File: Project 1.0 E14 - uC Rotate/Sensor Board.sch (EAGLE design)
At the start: 106 parts, among them IC1 LT1963EST-1.5, IC2 LT1963EST-1.5, IC4 LT1963EST-1.5, J1 501568-0207, J2 501568-0207, J3 SD-105027-101, J4 501568-0407, U1 MAG3110, U10 ADXL362, U11 TM4C1233H6PM, U14 TXB0108, U15 ADT7301, U17 LSM9DS0, U19 MAX21000, U2 H3LIS331DLTR, U21 SN74HC42, U22 SI7013, U3 L3GD20H, U4 LPS331AP, U5 MPL3115A2, U6 LSM303D, U8 STLM20, U9 LIS3DH, X1 32.768 kHz, X2 16.000 MHz

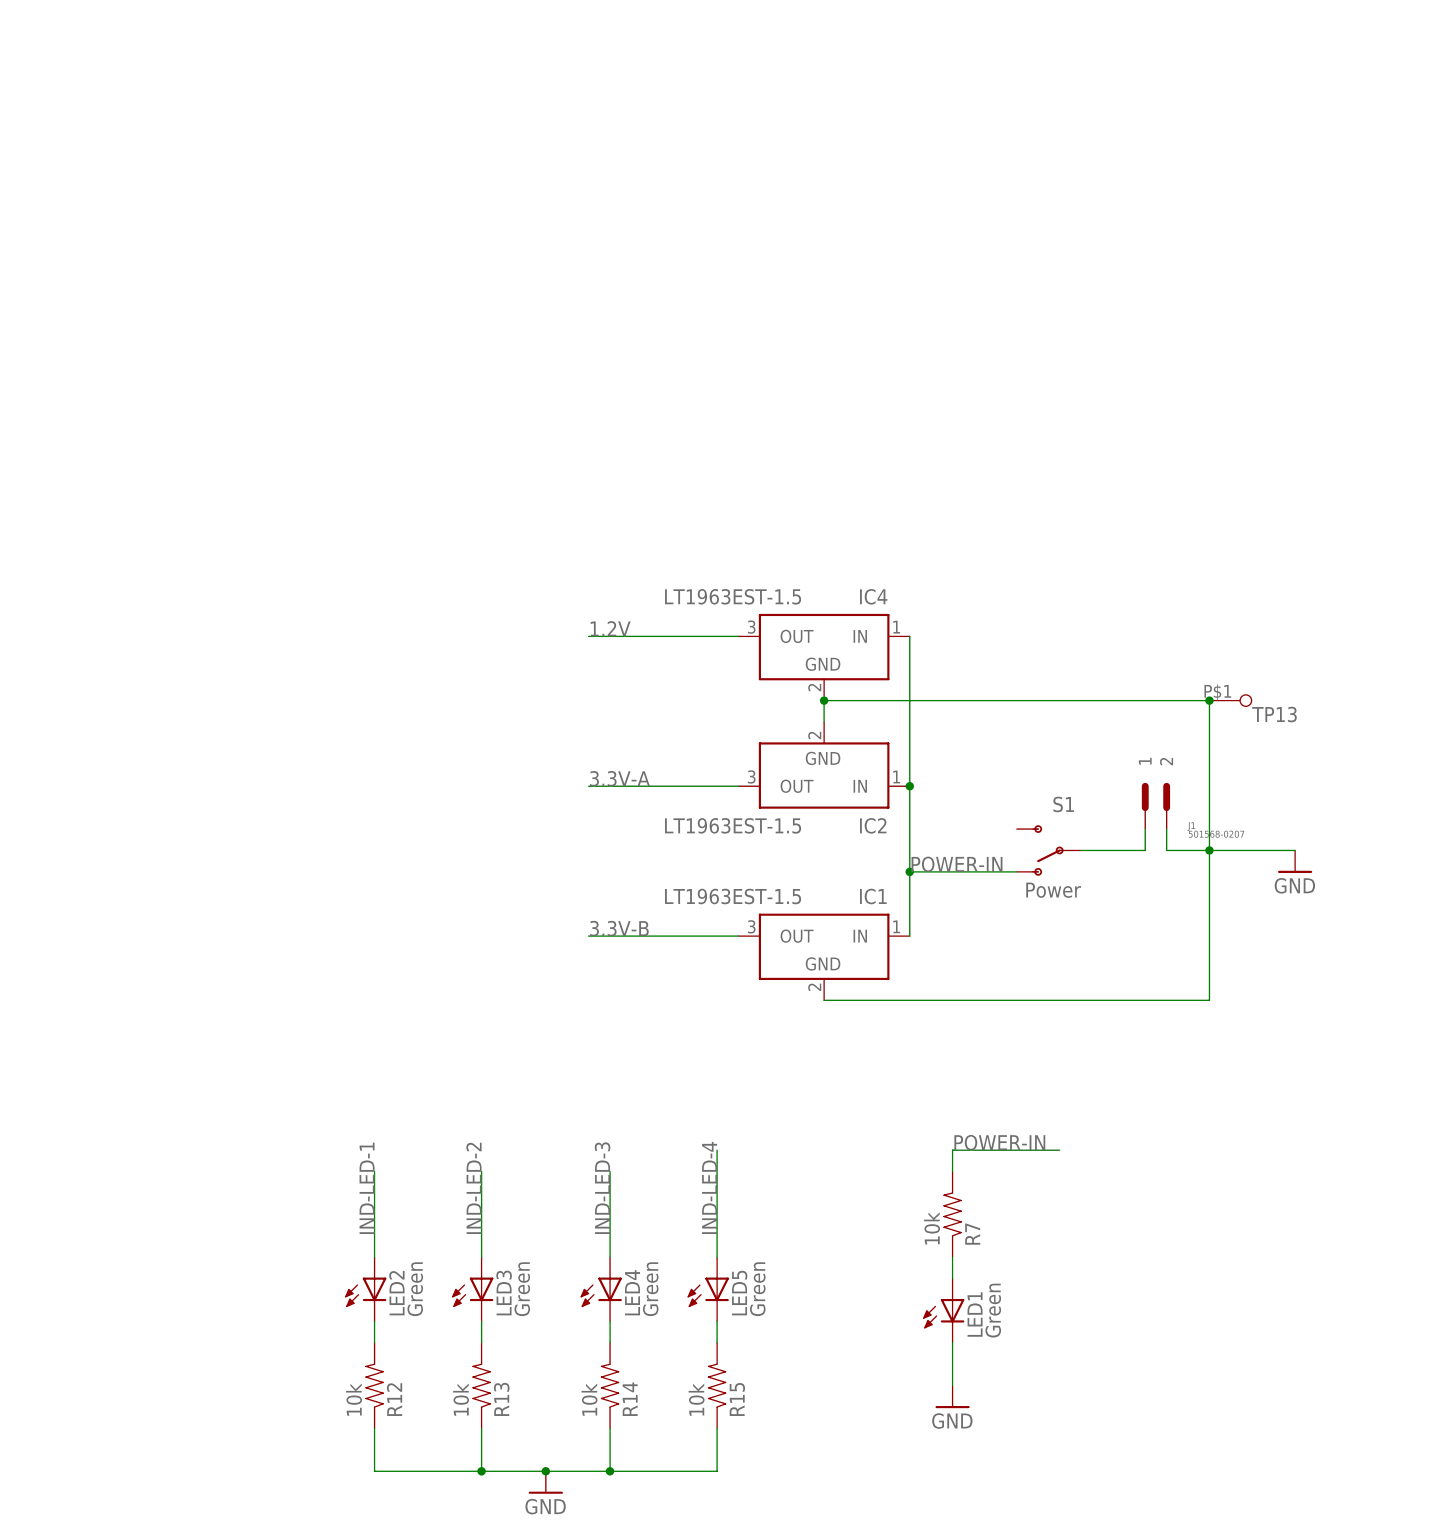
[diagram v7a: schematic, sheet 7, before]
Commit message: Sensor Test Board: Completed power routing, Removed 1.2V regulator as this is not needed per the Tiva c datasheet. Power regulators and their respective circuits have been added for both 3.3-A and 3.3-B power rails. Swich has been moved to the bottom layer and is now positined facing the bottom of the board.
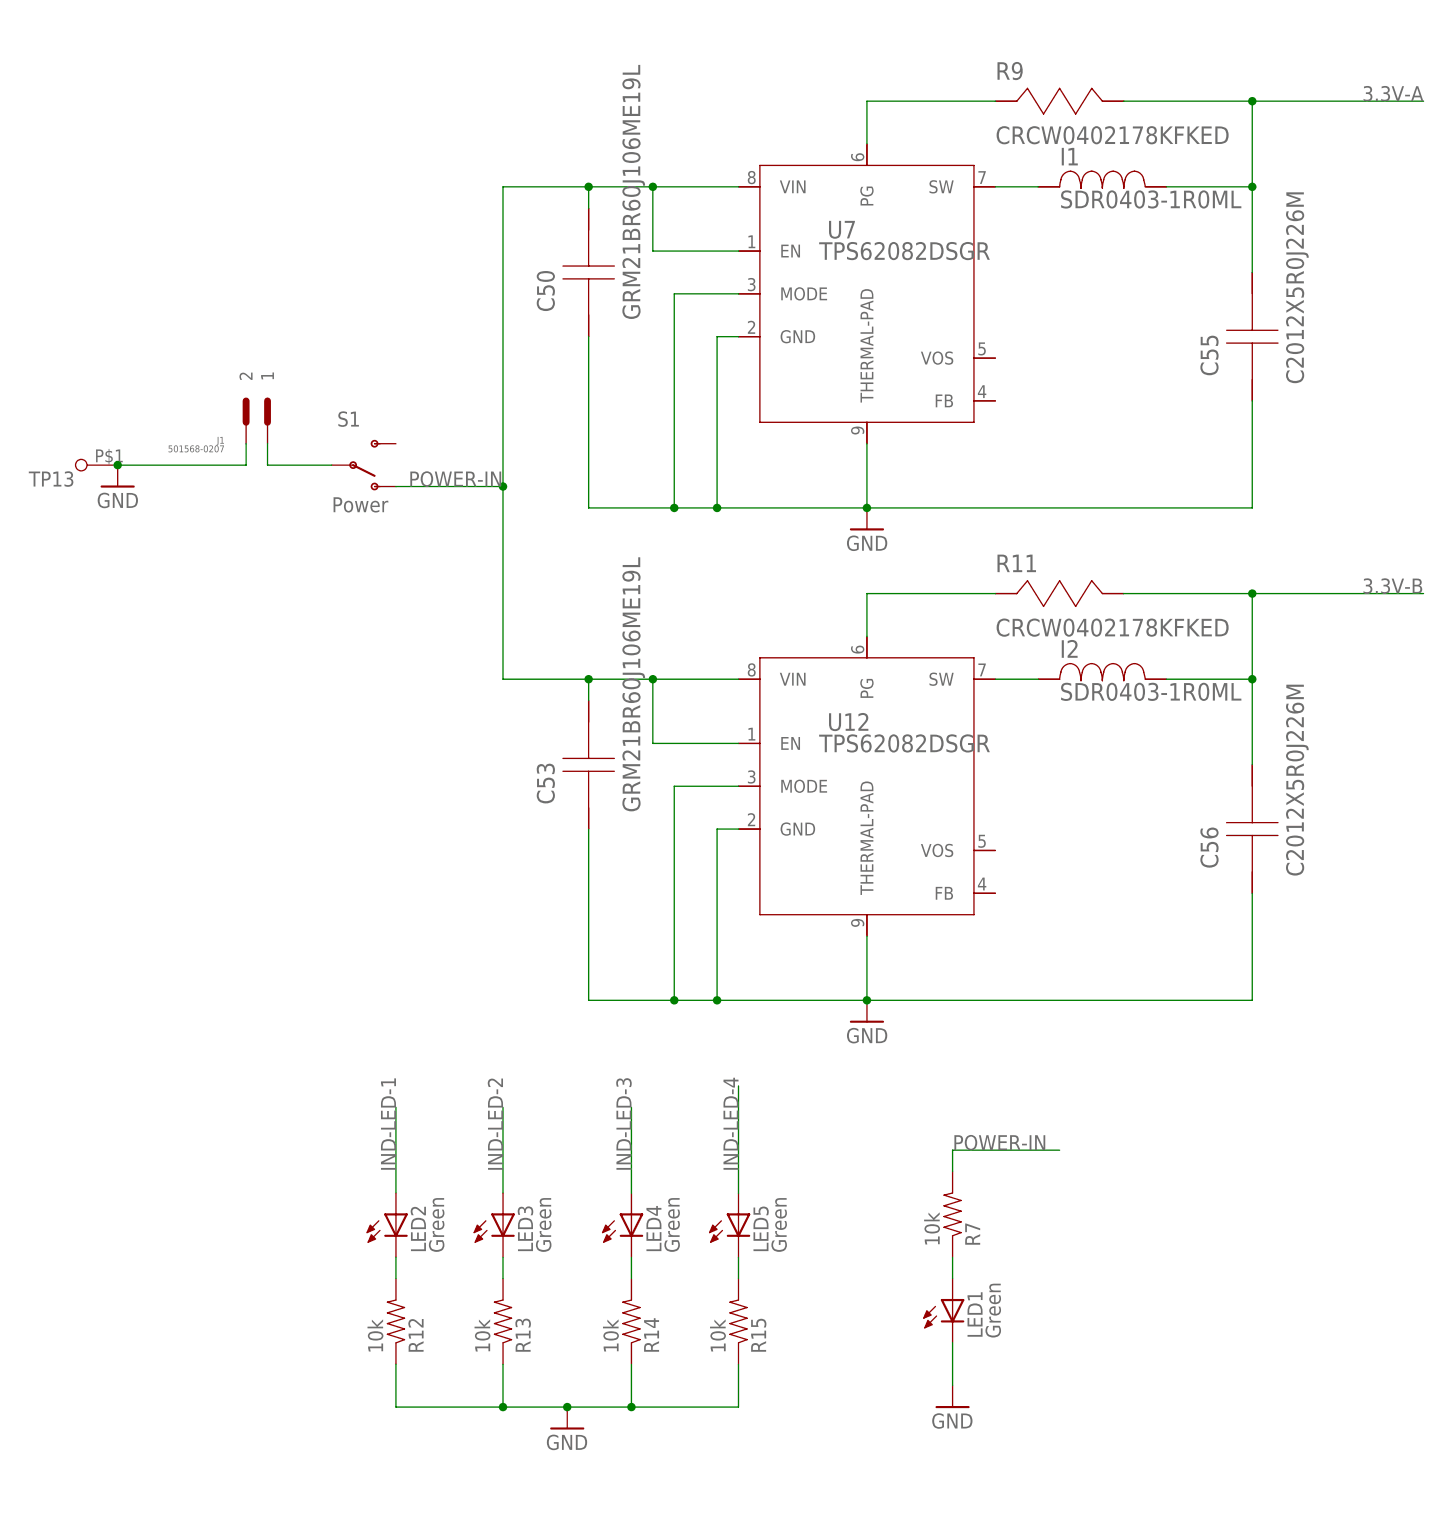
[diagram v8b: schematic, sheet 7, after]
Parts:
- removed IC1, IC2, IC4: LT1963EST-1.5, linear-technology:LT1963EST-1.5
- added C50, C53: GRM21BR60J106ME19L, Power Regulator:GRM21BR60J106ME19L
- added C55, C56: C2012X5R0J226M, Power Regulator:C2012X5R0J226M
- added I1, I2: SDR0403-1R0ML, Power Regulator:SDR0403-1R0ML
- added R11, R9: CRCW0402178KFKED, Power Regulator:CRCW0402178KFKED
- added U12, U7: TPS62082DSGR, Power Regulator:TPS62082DSGR
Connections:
- new net N$13: I1.2, U7.SW
- new net N$23: R9.2, U7.PG
- new net N$36: I2.2, U12.SW
- new net N$37: R11.2, U12.PG
- net 1.2V: no longer IC4G$1.OUT
- net 3.3V-A: now also C55.1, I1.1, R9.1; no longer IC2G$1.OUT
- net 3.3V-B: now also C56.1, I2.1, R11.1; no longer IC1G$1.OUT
- net GND: now also C50.2, C53.2, C55.2, C56.2, U12.GND, U12.MODE, U12.THERMAL-PAD, U7.GND, U7.MODE, U7.THERMAL-PAD; no longer IC1G$1.GND, IC2G$1.GND, IC4G$1.GND
- net POWER-IN: now also C50.1, C53.1, U12.EN, U12.VIN, U7.EN, U7.VIN; no longer IC1G$1.IN, IC2G$1.IN, IC4G$1.IN
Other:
- moved on the sheet: J1, LED2, LED3, LED4, LED5, R12, R13, R14, R15, S1, TP13
